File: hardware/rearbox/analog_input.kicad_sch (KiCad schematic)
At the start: 15 parts

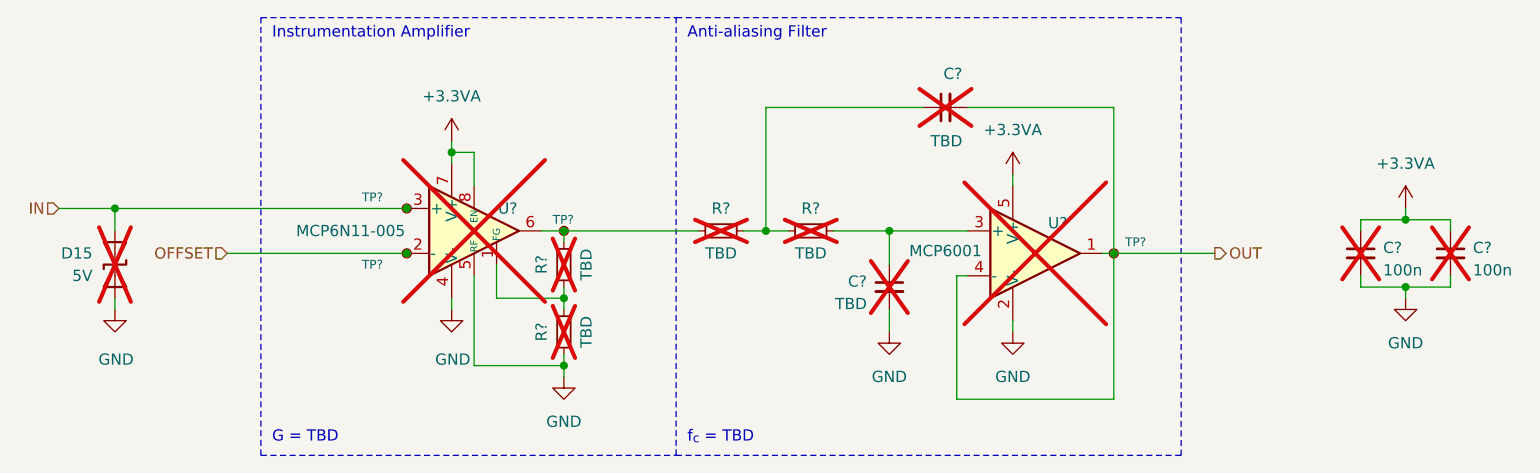
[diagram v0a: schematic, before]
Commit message: Place components on the PCB
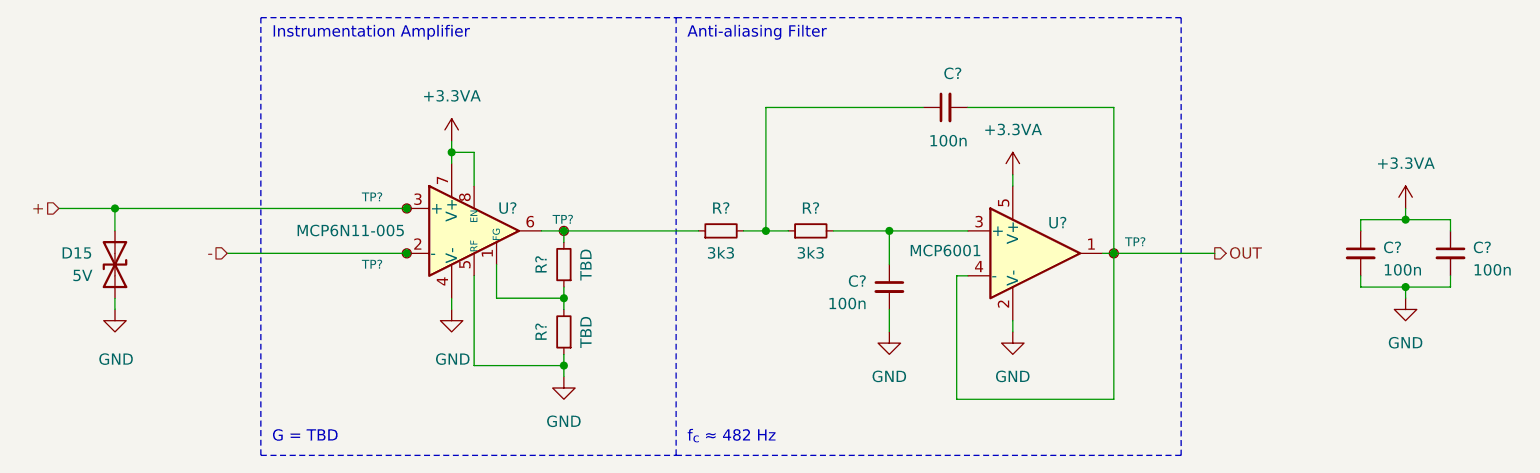
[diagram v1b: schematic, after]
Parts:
- removed C? (x2): TBD, Capacitor_SMD:C_0603_1608Metric, symbol Device:C_Small
- removed C? (x2): 100n, Capacitor_SMD:C_0603_1608Metric, symbol Device:C_Small
- removed R? (x4): TBD, Resistor_SMD:R_0603_1608Metric, symbol Device:R_Small
- removed TP? (x4): TestPoint_Small, TestPoint:TestPoint_Pad_D1.0mm, symbol Connector:TestPoint_Small
- removed U?: MCP6N11-005, Package_DFN_QFN:TDFN-8-1EP_3x2mm_P0.5mm_EP1.80x1.65mm, symbol MCP6N11:MCP6N11
- removed U?: MCP6001, Package_TO_SOT_SMD:SOT-23-5, symbol Amplifier_Operational:MCP6001-OT
- added C? (x4): 100n, Capacitor_SMD:C_0603_1608Metric, symbol Device:C_Small
- added R? (x2): 3k3, Resistor_SMD:R_0603_1608Metric, symbol Device:R_Small
- added R? (x2): TBD, Resistor_SMD:R_0603_1608Metric, symbol Device:R_Small
- added TP? (x4): TestPoint_Small, TestPoint:TestPoint_Pad_D1.0mm, symbol Connector:TestPoint_Small
- added U?: MCP6001, Package_TO_SOT_SMD:SOT-23-5, symbol Amplifier_Operational:MCP6001-OT
- added U?: MCP6N11-005, Package_DFN_QFN:TDFN-8-1EP_3x2mm_P0.5mm_EP1.80x1.65mm, symbol MCP6N11:MCP6N11
- D15: now fitted; now in the parts list
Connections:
- net +3.3VA: now also C?.1, C?.1, U?.5 (V+), U?.7 (V+), U?.8 (EN)
- net GND: now also C?.2, C?.2, C?.2, R?.1, U?.2 (V-), U?.4 (V-), U?.5 (RF), U?.9 (EP)
- net OUT: now also C?.2, TP?.1, U?.1, U?.4 (-)
- net IN renamed +
- net +: now also TP?.1, U?.3 (+)
- new net: R?.1, R?.2, TP?.1, U?.6
- new net: C?.1, R?.1, R?.2
- new net: C?.1, R?.2, U?.3 (+)
- new net: R?.1, R?.2, U?.1 (FG)
- new net -: TP?.1, U?.2 (-)
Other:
- note added: "f_{c} ≈ 482 Hz"
- note removed: "f_{c} = TBD"

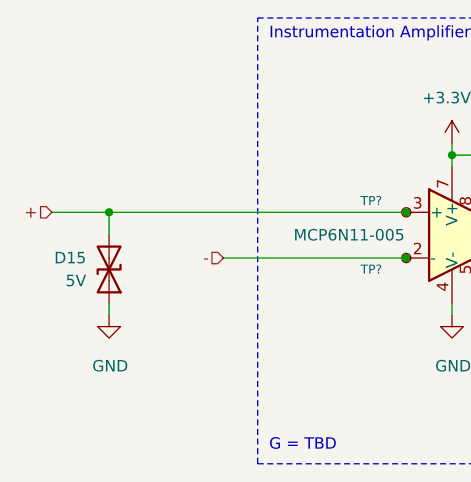
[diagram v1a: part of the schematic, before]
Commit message: Align footprint references
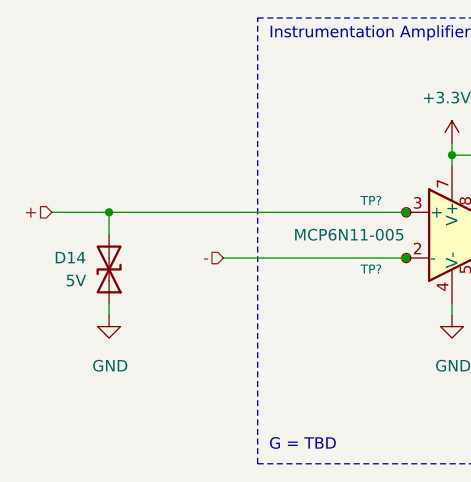
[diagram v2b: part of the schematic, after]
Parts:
- renumbered D15 to D14

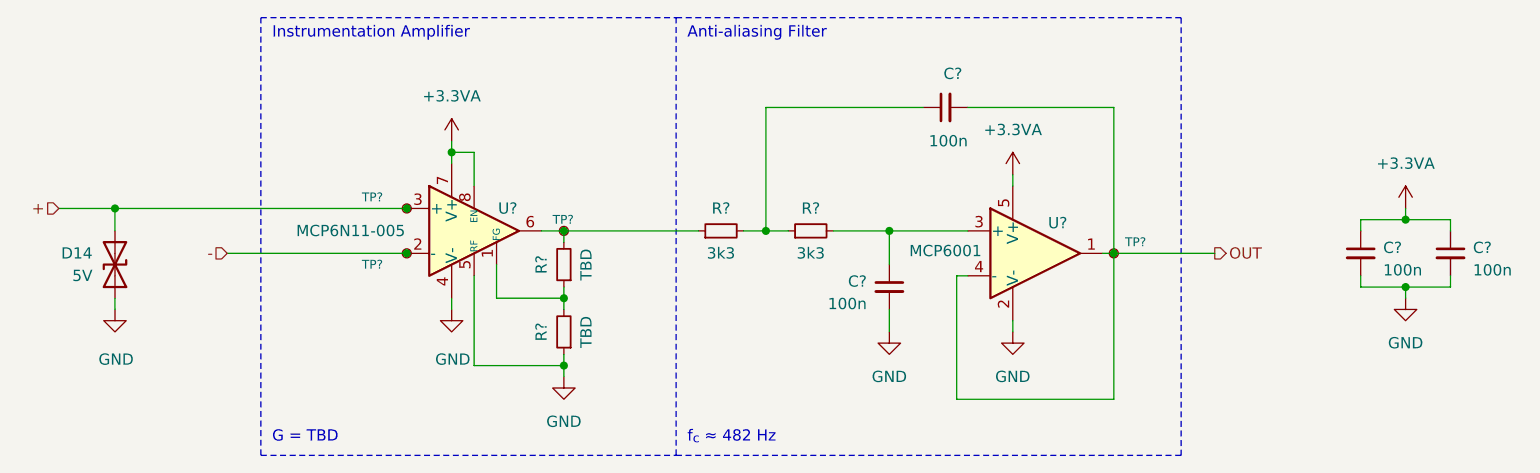
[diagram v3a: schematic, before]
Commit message: Route the tracks on the connector PCB
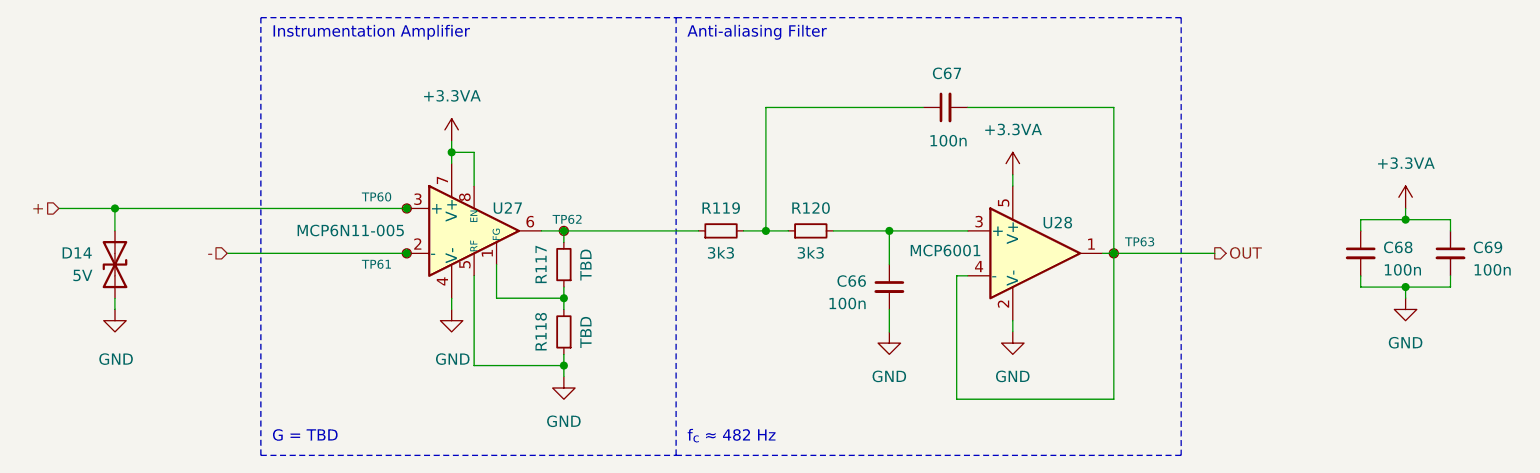
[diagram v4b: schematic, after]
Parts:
- gave numbers to parts that had none: 14

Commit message: Fix measurement bridges polarity
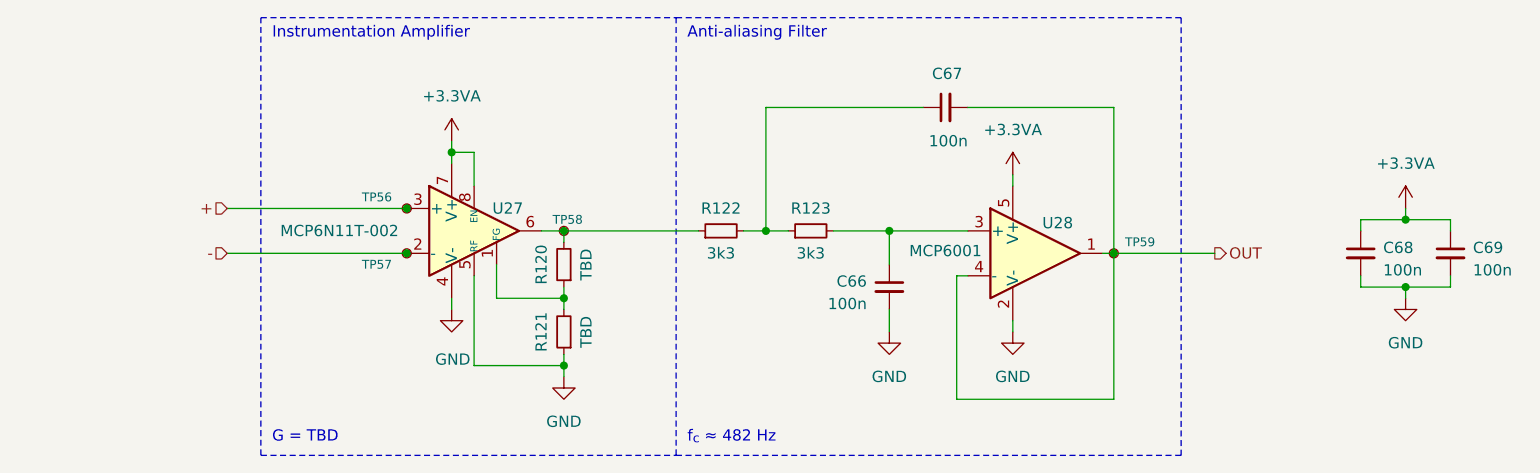
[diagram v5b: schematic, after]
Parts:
- removed D14: 5V, Diode_SMD:D_SOD-523, symbol Device:D_TVS
- U27: value MCP6N11-005 -> MCP6N11T-002; footprint Package_DFN_QFN:TDFN-8-1EP_3x2mm_P0.5mm_EP1.80x1.65mm -> Local_Library:TDFN-8-1EP_3x2mm_P0.5mm_EP1.80x1.65mm
- renumbered R117 to R120, R118 to R121, R119 to R122, R120 to R123, TP60 to TP56, TP61 to TP57, TP62 to TP58, TP63 to TP59
